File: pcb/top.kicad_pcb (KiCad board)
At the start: 2 copper layers, 186 x 20 mm, 0 parts

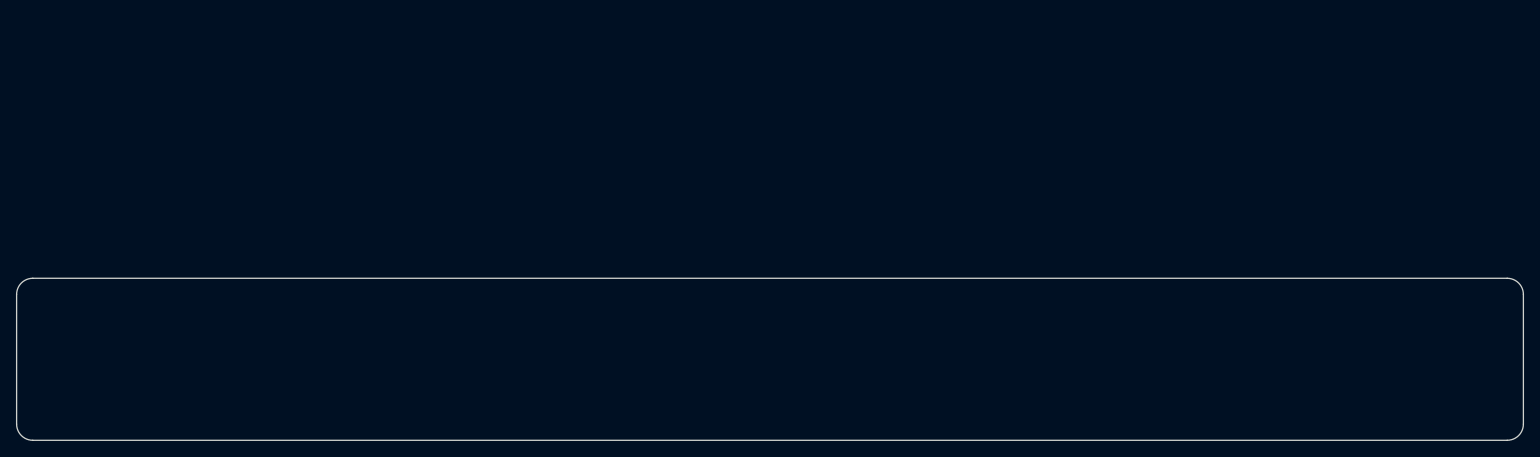
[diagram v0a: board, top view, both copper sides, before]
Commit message: Add LEDs package, position LEDs.
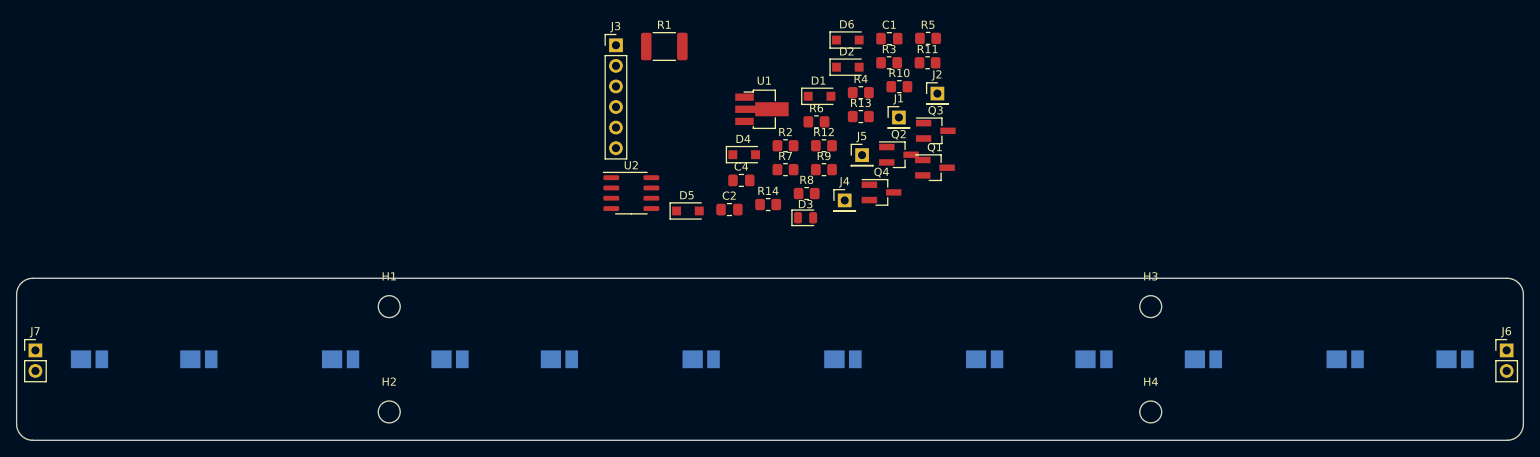
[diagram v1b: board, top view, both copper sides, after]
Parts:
- added C1: 22u/25V, Capacitor_SMD:C_0805_2012Metric_Pad1.18x1.45mm_HandSolder, F.Cu at (157.7, 50.4)
- added C2: 47u, Capacitor_SMD:C_0805_2012Metric_Pad1.18x1.45mm_HandSolder, F.Cu at (138.0, 71.5)
- added C4: 100n, Capacitor_SMD:C_0805_2012Metric_Pad1.18x1.45mm_HandSolder, F.Cu at (139.5, 67.9)
- added D1: 1N4007, Diode_SMD:D_SOD-123F, F.Cu at (149.1, 57.5)
- added D10: LED, LED_SMD:LED_PLCC_2835_Handsoldering, B.Cu at (169.5, 90.0)
- added D11: LED, LED_SMD:LED_PLCC_2835_Handsoldering, B.Cu at (90.0, 90.0)
- added D12: LED, LED_SMD:LED_PLCC_2835_Handsoldering, B.Cu at (183.0, 90.0)
- added D13: LED, LED_SMD:LED_PLCC_2835_Handsoldering, B.Cu at (103.5, 90.0)
- added D14: LED, LED_SMD:LED_PLCC_2835_Handsoldering, B.Cu at (196.5, 90.0)
- added D15: LED, LED_SMD:LED_PLCC_2835_Handsoldering, B.Cu at (117.0, 90.0)
- added D16: LED, LED_SMD:LED_PLCC_2835_Handsoldering, B.Cu at (214.0, 90.0)
- added D17: LED, LED_SMD:LED_PLCC_2835_Handsoldering, B.Cu at (134.5, 90.0)
- added D18: LED, LED_SMD:LED_PLCC_2835_Handsoldering, B.Cu at (227.6, 90.0)
- added D2: 1N4007, Diode_SMD:D_SOD-123F, F.Cu at (152.6, 53.9)
- added D3: CD4148W, Diode_SMD:D_0805_2012Metric, F.Cu at (147.4, 72.5)
- added D4: 1N4007, Diode_SMD:D_SOD-123F, F.Cu at (139.8, 64.7)
- added D5: 1N4007, Diode_SMD:D_SOD-123F, F.Cu at (132.9, 71.7)
- added D6: 1N4007, Diode_SMD:D_SOD-123F, F.Cu at (152.6, 50.6)
- added D7: LED, LED_SMD:LED_PLCC_2835_Handsoldering, B.Cu at (59.0, 90.0)
- added D8: LED, LED_SMD:LED_PLCC_2835_Handsoldering, B.Cu at (152.0, 90.0)
- added D9: LED, LED_SMD:LED_PLCC_2835_Handsoldering, B.Cu at (72.5, 90.0)
- added H1: MountingHole, MountingHole:MountingHole_2.7mm_M2.5, F.Cu at (96.0, 83.5)
- added H2: MountingHole, MountingHole:MountingHole_2.7mm_M2.5, F.Cu at (96.0, 96.5)
- added H3: MountingHole, MountingHole:MountingHole_2.7mm_M2.5, F.Cu at (190.0, 83.5)
- added H4: MountingHole, MountingHole:MountingHole_2.7mm_M2.5, F.Cu at (190.0, 96.5)
- added J1: Conn_01x01, Connector_PinHeader_2.54mm:PinHeader_1x01_P2.54mm_Vertical, F.Cu at (158.9, 60.1)
- added J2: Conn_01x01, Connector_PinHeader_2.54mm:PinHeader_1x01_P2.54mm_Vertical, F.Cu at (163.7, 57.2)
- added J3: Conn_01x06, Connector_PinHeader_2.54mm:PinHeader_1x06_P2.54mm_Vertical, F.Cu at (124.0, 51.2)
- added J4: Conn_01x01, Connector_PinHeader_2.54mm:PinHeader_1x01_P2.54mm_Vertical, F.Cu at (152.2, 70.4)
- added J5: Conn_01x01, Connector_PinHeader_2.54mm:PinHeader_1x01_P2.54mm_Vertical, F.Cu at (154.4, 64.8)
- added J6: Conn_01x02, Connector_PinHeader_2.54mm:PinHeader_1x02_P2.54mm_Vertical, F.Cu at (233.9, 88.9)
- added J7: Conn_01x02, Connector_PinHeader_2.54mm:PinHeader_1x02_P2.54mm_Vertical, F.Cu at (52.3, 88.9)
- added Q1: 2N7002, Package_TO_SOT_SMD:SOT-23_Handsoldering, F.Cu at (163.4, 66.3)
- added Q2: 2N7002, Package_TO_SOT_SMD:SOT-23_Handsoldering, F.Cu at (158.9, 64.7)
- added Q3: 2N7002, Package_TO_SOT_SMD:SOT-23_Handsoldering, F.Cu at (163.5, 61.8)
- added Q4: 2N7002, Package_TO_SOT_SMD:SOT-23_Handsoldering, F.Cu at (156.8, 69.4)
- added R1: 100R, Resistor_SMD:R_1812_4532Metric_Pad1.30x3.40mm_HandSolder, F.Cu at (130.0, 51.4)
- added R10: 10k, Resistor_SMD:R_0805_2012Metric_Pad1.20x1.40mm_HandSolder, F.Cu at (159.0, 56.3)
- added R11: 22k, Resistor_SMD:R_0805_2012Metric_Pad1.20x1.40mm_HandSolder, F.Cu at (162.5, 53.4)
- added R12: 10k, Resistor_SMD:R_0805_2012Metric_Pad1.20x1.40mm_HandSolder, F.Cu at (149.7, 63.6)
- added R13: 10k, Resistor_SMD:R_0805_2012Metric_Pad1.20x1.40mm_HandSolder, F.Cu at (154.2, 60.0)
- added R14: 10k, Resistor_SMD:R_0805_2012Metric_Pad1.20x1.40mm_HandSolder, F.Cu at (142.8, 70.9)
- added R2: 2k2, Resistor_SMD:R_0805_2012Metric_Pad1.20x1.40mm_HandSolder, F.Cu at (144.9, 63.6)
- added R3: R, Resistor_SMD:R_0805_2012Metric_Pad1.20x1.40mm_HandSolder, F.Cu at (157.7, 53.4)
- added R4: R, Resistor_SMD:R_0805_2012Metric_Pad1.20x1.40mm_HandSolder, F.Cu at (154.2, 57.1)
- added R5: R, Resistor_SMD:R_0805_2012Metric_Pad1.20x1.40mm_HandSolder, F.Cu at (162.5, 50.4)
- added R6: R, Resistor_SMD:R_0805_2012Metric_Pad1.20x1.40mm_HandSolder, F.Cu at (148.7, 60.7)
- added R7: 10k, Resistor_SMD:R_0805_2012Metric_Pad1.20x1.40mm_HandSolder, F.Cu at (144.9, 66.6)
- added R8: R, Resistor_SMD:R_0805_2012Metric_Pad1.20x1.40mm_HandSolder, F.Cu at (147.5, 69.5)
- added R9: R, Resistor_SMD:R_0805_2012Metric_Pad1.20x1.40mm_HandSolder, F.Cu at (149.7, 66.6)
- added U1: L78L05_SOT89, Package_TO_SOT_SMD:SOT-89-3_Handsoldering, F.Cu at (142.0, 59.1)
- added U2: PIC12F629-ISN, Package_SO:SOIC-8_3.9x4.9mm_P1.27mm, F.Cu at (125.9, 69.5)

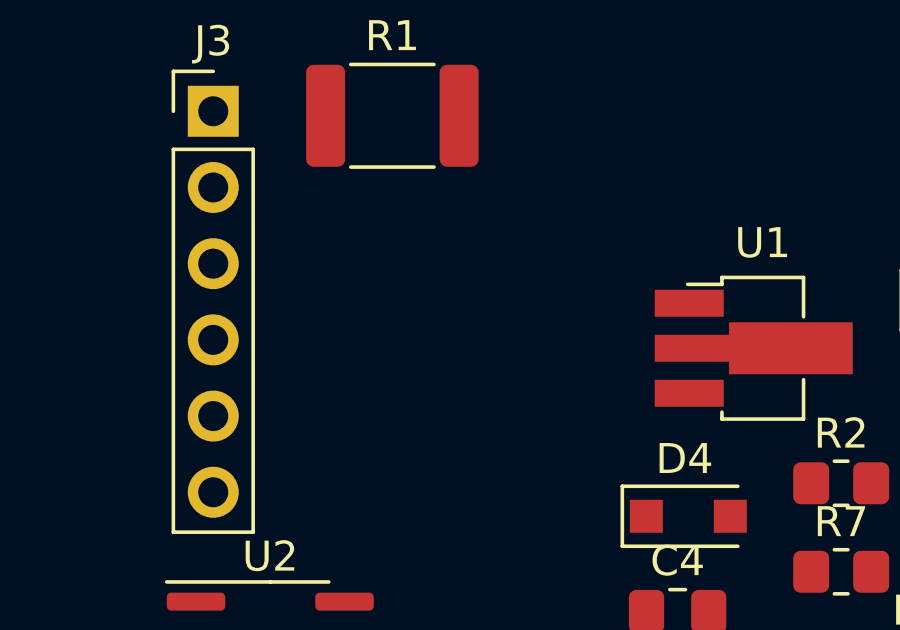
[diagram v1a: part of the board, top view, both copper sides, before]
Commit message: Add MOSFET gate protection resistors.
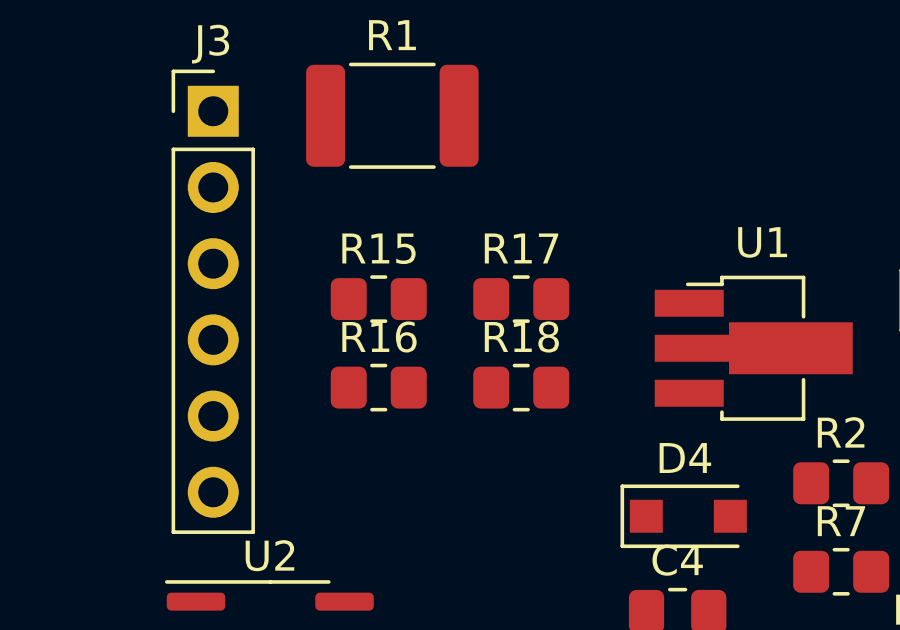
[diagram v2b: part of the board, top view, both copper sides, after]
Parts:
- added R15: 250R, Resistor_SMD:R_0805_2012Metric_Pad1.20x1.40mm_HandSolder, F.Cu at (129.5, 57.5)
- added R16: 250R, Resistor_SMD:R_0805_2012Metric_Pad1.20x1.40mm_HandSolder, F.Cu at (129.5, 60.5)
- added R17: 250R, Resistor_SMD:R_0805_2012Metric_Pad1.20x1.40mm_HandSolder, F.Cu at (134.2, 57.5)
- added R18: 250R, Resistor_SMD:R_0805_2012Metric_Pad1.20x1.40mm_HandSolder, F.Cu at (134.2, 60.5)
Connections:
- Q1 pad 1: GP0|PGD -> Net-(Q1-Pad1)
- Q3 pad 1: GP1|PGC -> Net-(Q3-Pad1)
- R10 pad 2: GP0|PGD -> Net-(Q1-Pad1)
- R13 pad 2: GP1|PGC -> Net-(Q3-Pad1)
- U2 pad 2: Net-(Q4-Pad1) -> Net-(R18-Pad1)
- U2 pad 3: Net-(Q2-Pad1) -> Net-(R16-Pad1)

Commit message: Add proper PCB dimensions.
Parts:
- added C3: 470u/25V, Capacitor_THT:CP_Radial_D8.0mm_P3.50mm, F.Cu at (85.5, 99.8)
- added C5: 1000u/25V, Capacitor_THT:CP_Radial_D10.0mm_P5.00mm, F.Cu at (85.5, 99.8)
- added J10: Conn_01x01, Connector_PinHeader_2.54mm:PinHeader_1x01_P2.54mm_Vertical, B.Cu at (82.0, 98.5)
- added J11: Conn_01x01, Connector_PinHeader_2.54mm:PinHeader_1x01_P2.54mm_Vertical, B.Cu at (82.0, 95.5)
- added J8: Conn_01x01, TestPoint:TestPoint_THTPad_D1.5mm_Drill0.7mm, F.Cu at (52.0, 86.5)
- added J9: Conn_01x01, TestPoint:TestPoint_THTPad_D1.5mm_Drill0.7mm, F.Cu at (234.0, 86.5)
- added L1: 47uH, Inductor_THT:L_Axial_L6.6mm_D2.7mm_P10.16mm_Horizontal_Vishay_IM-2, F.Cu at (-64.0, 96.5)
- J1, J2, J4, J5: moved to B.Cu
- J6, J7: value Conn_01x02 -> Conn_01x01; footprint Connector_PinHeader_2.54mm:PinHeader_1x02_P2.54mm_Vertical -> TestPoint:TestPoint_THTPad_D1.5mm_Drill0.7mm
- moved J6 182.0 mm to (52.0, 93.5)
- moved J7 181.7 mm to (234.0, 93.5)
- moved C1 150.7 mm to (10.2, 81.4)
- moved C2 150.7 mm to (-9.51, 102.5)
- moved C4 150.7 mm to (-8.04, 98.9)
- moved D1 150.7 mm to (1.62, 88.5)
- moved D2 150.7 mm to (5.11, 84.9)
- moved D3 150.7 mm to (-0.11, 103.5)
- moved D4 150.7 mm to (-7.68, 95.7)
- moved D5 150.7 mm to (-14.6, 102.7)
- moved D6 150.7 mm to (5.11, 81.6)
- moved J3 150.7 mm to (-23.5, 82.2)
- moved Q1 150.7 mm to (15.9, 97.3)
- moved Q2 150.7 mm to (11.4, 95.7)
- moved Q3 150.7 mm to (16.0, 92.8)
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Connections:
- J7 pad 1: Net-(J7-Pad1) -> +15V
- R2 pad 2: (no net) -> Net-(C3-Pad2)
- R8 pad 2: Net-(J6-Pad2) -> Net-(J8-Pad1)
- R9 pad 2: Net-(J7-Pad1) -> Net-(J9-Pad1)
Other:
- board size 186 x 20 mm -> 186 x 28 mm

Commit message: Wire part of PCB.
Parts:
- C3, C5: moved to B.Cu
- moved R18 210.5 mm to (197.1, 82.8)
- moved R9 206.3 mm to (207.8, 81.3)
- moved R14 203.0 mm to (197.1, 79.8)
- moved Q4 194.1 mm to (202.4, 81.3)
- moved D5 188.1 mm to (173.2, 93.5), turned to 90 degrees
- moved D4 177.9 mm to (170.2, 93.5), turned to 270 degrees
- moved R17 174.1 mm to (160.8, 82.3), turned to 180 degrees
- moved D1 168.9 mm to (170.2, 98.8), turned to 90 degrees
- moved D2 168.7 mm to (173.2, 98.8), turned to 270 degrees
- moved R4 167.7 mm to (174.2, 80.8), turned to 180 degrees
- moved D3 166.1 mm to (165.9, 96.4), turned to 90 degrees
- moved U2 165.9 mm to (143.8, 87.8)
- moved R3 164.4 mm to (174.5, 77.5), turned to 180 degrees
- moved U1 162.8 mm to (157.2, 96.0), turned to 90 degrees
- moved J3 162.4 mm to (138.2, 97.5), turned to 90 degrees
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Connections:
- D10 pad 2: Net-(D10-Pad2) -> +15V
- D16 pad 1: Net-(D15-Pad1) -> Net-(D16-Pad1)
- D18 pad 1: Net-(D17-Pad1) -> Net-(D18-Pad1)
- D7 pad 2: Net-(D7-Pad2) -> +15V
- D8 pad 2: Net-(D8-Pad2) -> +15V
- D9 pad 2: Net-(D9-Pad2) -> +15V
- Q1 pad 3: Net-(D17-Pad1) -> Net-(Q1-Pad3)
- Q3 pad 3: Net-(D15-Pad1) -> Net-(Q3-Pad3)
- R3 pad 1: +15V -> Net-(D15-Pad1)
- R3 pad 2: Net-(D7-Pad2) -> Net-(Q3-Pad3)
- R4 pad 1: +15V -> Net-(D16-Pad1)
- R4 pad 2: Net-(D8-Pad2) -> Net-(Q3-Pad3)
- R5 pad 1: +15V -> Net-(D17-Pad1)
- R5 pad 2: Net-(D9-Pad2) -> Net-(Q1-Pad3)
- R6 pad 1: +15V -> Net-(D18-Pad1)
- R6 pad 2: Net-(D10-Pad2) -> Net-(Q1-Pad3)
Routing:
- net K: track 0.00 -> 170.6 mm, vias 0 -> 2
- net /J: track 0.00 -> 162.5 mm, vias 0 -> 2
- net Net-(D18-Pad1): track 0.00 -> 57.8 mm
- net Net-(D16-Pad1): track 0.00 -> 44.7 mm
- net Net-(R16-Pad1): track 0.00 -> 40.0 mm
- net Net-(D13-Pad1): track 0.00 -> 32.7 mm
- net Net-(D11-Pad2): track 0.00 -> 32.7 mm
- net Net-(D14-Pad1): track 0.00 -> 32.3 mm
- net Net-(D12-Pad1): track 0.00 -> 31.3 mm
- net Net-(D13-Pad2): track 0.00 -> 31.3 mm
- net Net-(D12-Pad2): track 0.00 -> 30.4 mm
- net Net-(J9-Pad1): track 0.00 -> 28.7 mm
- net Net-(D11-Pad1): track 0.00 -> 28.4 mm
- net Net-(D10-Pad1): track 0.00 -> 28.1 mm
- net Net-(R18-Pad1): track 0.00 -> 27.8 mm
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- added copper zone on B.Cu, net +15V
- added copper zone on F.Cu, net GND

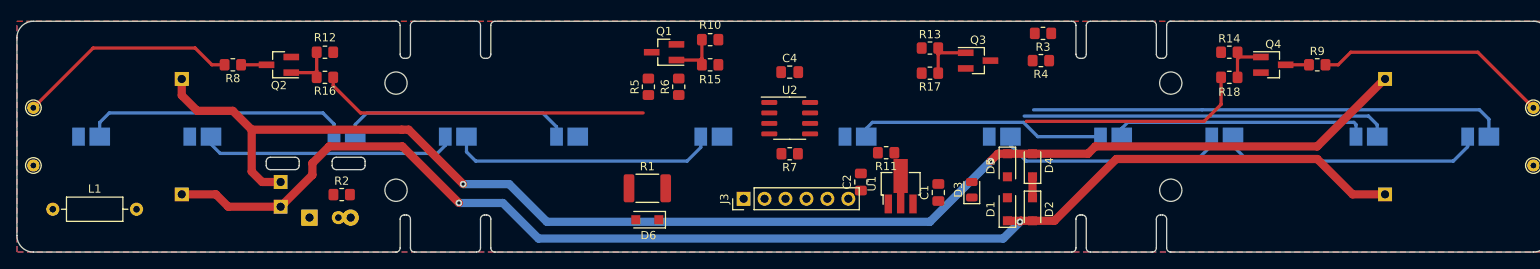
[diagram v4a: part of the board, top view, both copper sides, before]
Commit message: Wire whole PCB.
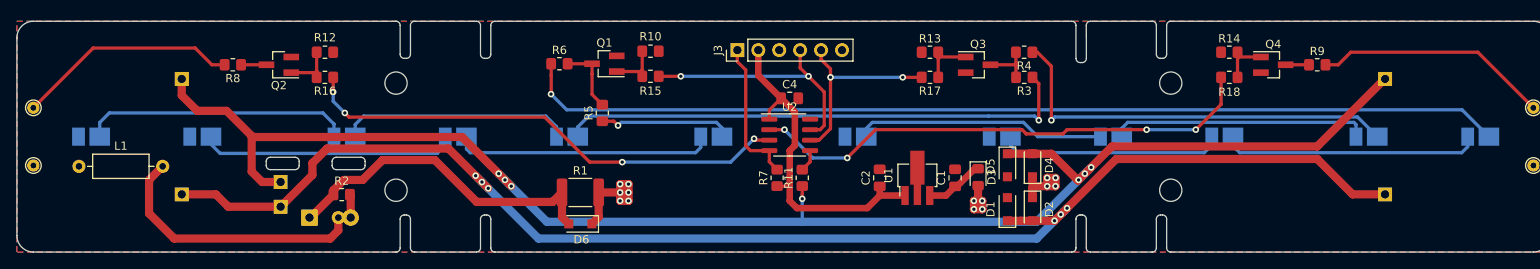
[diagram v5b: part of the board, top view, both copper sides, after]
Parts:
- D3: footprint Diode_SMD:D_0805_2012Metric -> Diode_SMD:D_0805_2012Metric_Pad1.15x1.40mm_HandSolder
- moved J3 18.1 mm to (137.4, 79.5)
- moved R6 14.7 mm to (115.8, 81.2), turned to 0 degrees
- moved R11 10.6 mm to (145.3, 95.0), turned to 90 degrees
- moved D6 8.14 mm to (118.4, 100.6)
- moved R1 8.14 mm to (118.4, 96.8)
- moved Q1 7.37 mm to (121.3, 81.2)
- moved R10 7.37 mm to (126.9, 79.6)
- moved R15 7.37 mm to (126.9, 82.7)
- moved R5 6.43 mm to (121.0, 87.1)
- moved L1 6.10 mm to (57.5, 93.6)
- moved R3 5.80 mm to (172.2, 82.8)
- moved R7 3.29 mm to (142.2, 95.0), turned to 90 degrees
- moved C4 3.17 mm to (143.8, 85.3)
- moved C1 2.70 mm to (163.8, 95.0)
- moved C2 2.34 mm to (154.7, 95.0)
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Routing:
- net Net-(D15-Pad1): track 0.00 -> 63.4 mm, vias 0 -> 1
- net Net-(D18-Pad1): track 57.8 -> 119.6 mm, vias 0 -> 1
- net VCC: track 0.00 -> 41.4 mm
- net Net-(C3-Pad1): track 0.00 -> 40.6 mm
- net Net-(C3-Pad2): track 1.50 -> 36.9 mm
- net Net-(R18-Pad1): track 27.8 -> 62.6 mm, vias 0 -> 4
- net +15V: track 2.53 -> 34.2 mm, vias 0 -> 14
- net GP0|PGD: track 0.00 -> 30.5 mm, vias 0 -> 2
- net GP1|PGC: track 0.00 -> 24.1 mm, vias 0 -> 2
- net Net-(R16-Pad1): track 40.0 -> 60.1 mm, vias 0 -> 4
- net K: track 170.6 -> 188.5 mm, vias 2 -> 7
- net GP3|MCLR: track 0.00 -> 17.8 mm
- net Net-(D17-Pad1): track 0.00 -> 16.2 mm, vias 0 -> 1
- net Net-(Q1-Pad3): track 0.00 -> 8.45 mm
- net /J: track 162.5 -> 170.7 mm, vias 2 -> 6
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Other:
- outline, holes or cut-outs redrawn

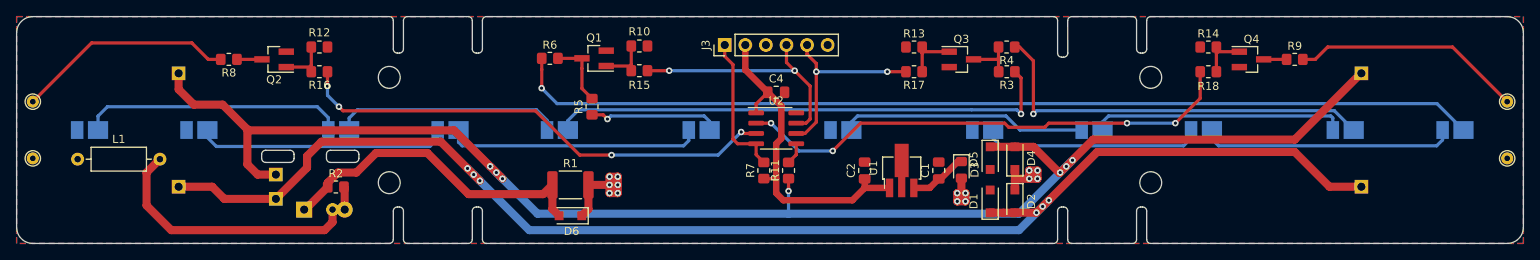
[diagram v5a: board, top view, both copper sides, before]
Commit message: Tweak silkscreen etc.
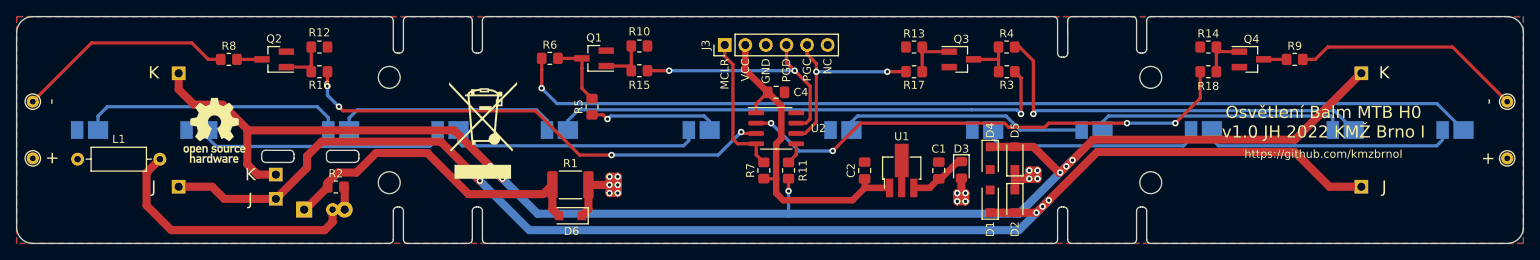
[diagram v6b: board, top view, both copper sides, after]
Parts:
- added REF**: OSHW-Logo_7.5x8mm_SilkScreen, Symbol:OSHW-Logo_7.5x8mm_SilkScreen, F.Cu at (74.4, 90.0)
- added REF**: WEEE-Logo_8.4x12mm_SilkScreen, Symbol:WEEE-Logo_8.4x12mm_SilkScreen, F.Cu at (107.6, 90.0)
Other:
- board text added: "+"
- board text added: "-"
- board text added: "GND"
- board text added: "J"
- board text added: "K"
- board text added: "MCLR"
- board text added: "NC"
- board text added: "Osvětlení Balm MTB H0 v1.0 JH 2022 KMŽ Brno I"
- board text added: "PGC"
- board text added: "PGD"
- board text added: "VCC"
- board text added: "https://github.com/kmzbrnoI"
